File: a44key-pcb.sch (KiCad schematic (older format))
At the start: 61 parts, among them J1 AudioJack3, SW1 SW_Push, U1 ATmega32U4-AU, Y1 16MHz

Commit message: Added raisers for the thumbs
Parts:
- added J2, J3: Conn_01x04_Female, Connector_PinHeader_2.54mm:PinHeader_1x04_P2.54mm_Vertical, symbol Connector:Conn_01x04_Female
- J1: symbol SJ-43514:SJ-43514 -> a44key-pcb-rescue:SJ-43514-SJ-43514
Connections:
- net COL4: now also J2.2 (Pin_2)
- net COL5: now also J2.3 (Pin_3)
- net GND: now also Y1.2, Y1.4; no longer Y1.1, Y1.3
- net at C3.1, U1.16 (XTAL2): now also Y1.3; no longer Y1.2
- net at C2.1, U1.17 (XTAL1): now also Y1.1; no longer Y1.4
- net TH35: now reaches D4.2 (A), MX4.2 (ROW)
- net TH35: now also J3.2 (Pin_2)
- net TH34: now reaches D8.2 (A), MX8.2 (ROW)
- net TH34: now also J3.3 (Pin_3)
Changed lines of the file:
@@
 Wire Wire Line
 	3000 3050 2700 3050
-$Comp
-L Device:Crystal_GND24_Small Y1
-U 1 1 616C3379
-P 2150 2550
-F 0 "Y1" H 2294 2596 50  0000 L CNN
-F 1 "16MHz" H 2294 2505 50  0000 L CNN
-F 2 "Crystal:Crystal_SMD_3225-4Pin_3.2x2.5mm_HandSoldering" H 2150 2550 50  0001 C CNN
-F 3 "~" H 2150 2550 50  0001 C CNN
-	1    2150 2550
-	1    0    0    -1
-$EndComp
 Wire Wire Line
 	3000 2450 2150 2450
@@
 ROW3
 $Comp
-L SJ-43514:SJ-43514 J1
+L a44key-pcb-rescue:SJ-43514-SJ-43514 J1
 U 1 1 6186D5DF
 P 3850 850
@@
 	6450 1200 6750 1200
 $Comp
-L power:+5V #PWR?
+L power:+5V #PWR0115
 U 1 1 617476F1
 P 4500 750
-F 0 "#PWR?" H 4500 600 50  0001 C CNN
+F 0 "#PWR0115" H 4500 600 50  0001 C CNN
 F 1 "+5V" H 4515 923 50  0000 C CNN
 F 2 "" H 4500 750 50  0001 C CNN
@@
 Wire Wire Line
 	4250 750  4500 750
+$Comp
+L Device:Crystal_GND24_Small Y1
+U 1 1 616C3379
+P 2150 2550
+F 0 "Y1" H 2294 2596 50  0000 L CNN
+F 1 "16MHz" H 2294 2505 50  0000 L CNN
+F 2 "Crystal:Crystal_SMD_3225-4Pin_3.2x2.5mm_HandSoldering" H 2150 2550 50  0001 C CNN
+F 3 "~" H 2150 2550 50  0001 C CNN
+	1    2150 2550
+	0    1    1    0
+$EndComp
+$Comp
+L Connector:Conn_01x04_Female J2
+U 1 1 6193A042
+P 6750 5700
+F 0 "J2" H 6642 5275 50  0000 C CNN
+F 1 "Conn_01x04_Female" H 6642 5366 50  0000 C CNN
+F 2 "Connector_PinHeader_2.54mm:PinHeader_1x04_P2.54mm_Vertical" H 6750 5700 50  0001 C CNN
+F 3 "~" H 6750 5700 50  0001 C CNN
+	1    6750 5700
+	1    0    0    1
+$EndComp
+$Comp
+L Connector:Conn_01x04_Female J3
+U 1 1 6193AE0A
+P 8500 5650
+F 0 "J3" H 8528 5626 50  0000 L CNN
+F 1 "Conn_01x04_Female" H 8528 5535 50  0000 L CNN
+F 2 "Connector_PinHeader_2.54mm:PinHeader_1x04_P2.54mm_Vertical" H 8500 5650 50  0001 C CNN
+F 3 "~" H 8500 5650 50  0001 C CNN
+	1    8500 5650
+	1    0    0    -1
+$EndComp
+Text GLabel 6150 5600 0    50   Input ~ 0
+COL5
+Text GLabel 6150 5700 0    50   Input ~ 0
+COL4
+Wire Wire Line
+	6150 5600 6550 5600
+Wire Wire Line
+	6150 5700 6550 5700
+Text GLabel 8000 5650 0    50   Input ~ 0
+TH35
+Text GLabel 8000 5750 0    50   Input ~ 0
+TH34
+Wire Wire Line
+	8000 5650 8300 5650
+Wire Wire Line
+	8000 5750 8300 5750
+Text GLabel 6300 4800 0    50   Input ~ 0
+TH35
+Wire Wire Line
+	6300 4800 6500 4800
+Wire Wire Line
+	6500 4800 6500 4900
+Wire Wire Line
+	6500 4900 6550 4900
+Connection ~ 6550 4900
+Text GLabel 7100 4850 0    50   Input ~ 0
+TH34
+Wire Wire Line
+	7100 4850 7250 4850
+Wire Wire Line
+	7250 4850 7250 4900
+Connection ~ 7250 4900
 $EndSCHEMATC

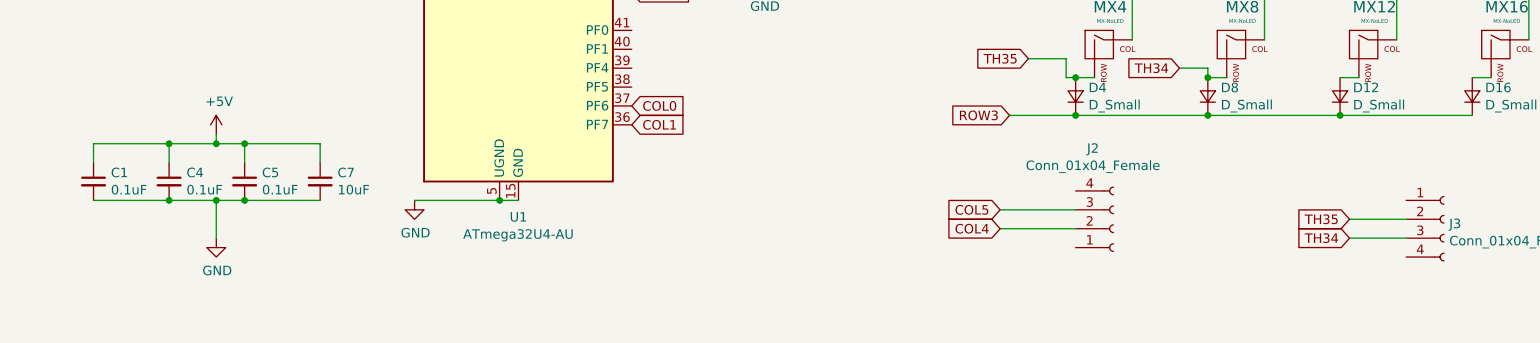
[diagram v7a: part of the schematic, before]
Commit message: Rerouting
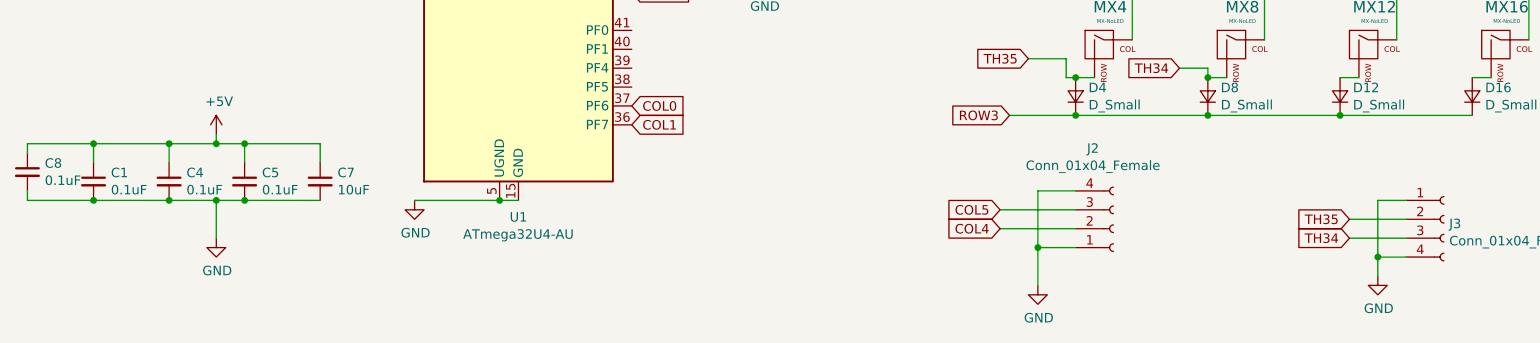
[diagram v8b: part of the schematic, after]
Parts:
- added C8: 0.1uF, Capacitor_SMD:C_0805_2012Metric, symbol Device:C_Small
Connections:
- net +5V: now also C8.1
- net GND: now also J2.1 (Pin_1), J2.4 (Pin_4), J3.1 (Pin_1), J3.4 (Pin_4), C8.2
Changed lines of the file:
@@
 	7250 4850 7250 4900
 Connection ~ 7250 4900
+$Comp
+L Device:C_Small C8
+U 1 1 6197A27B
+P 1000 5400
+F 0 "C8" H 1092 5446 50  0000 L CNN
+F 1 "0.1uF" H 1092 5355 50  0000 L CNN
+F 2 "Capacitor_SMD:C_0805_2012Metric" H 1000 5400 50  0001 C CNN
+F 3 "~" H 1000 5400 50  0001 C CNN
+	1    1000 5400
+	1    0    0    -1
+$EndComp
+Wire Wire Line
+	1350 5550 1000 5550
+Wire Wire Line
+	1000 5550 1000 5500
+Connection ~ 1350 5550
+Wire Wire Line
+	1350 5250 1000 5250
+Wire Wire Line
+	1000 5250 1000 5300
+Connection ~ 1350 5250
+$Comp
+L power:GND #PWR?
+U 1 1 61993731
+P 6350 6000
+F 0 "#PWR?" H 6350 5750 50  0001 C CNN
+F 1 "GND" H 6355 5827 50  0000 C CNN
+F 2 "" H 6350 6000 50  0001 C CNN
+F 3 "" H 6350 6000 50  0001 C CNN
+	1    6350 6000
+	1    0    0    -1
+$EndComp
+$Comp
+L power:GND #PWR?
+U 1 1 61993FD0
+P 8150 5950
+F 0 "#PWR?" H 8150 5700 50  0001 C CNN
+F 1 "GND" H 8155 5777 50  0000 C CNN
+F 2 "" H 8150 5950 50  0001 C CNN
+F 3 "" H 8150 5950 50  0001 C CNN
+	1    8150 5950
+	1    0    0    -1
+$EndComp
+Wire Wire Line
+	8300 5550 8150 5550
+Wire Wire Line
+	8150 5550 8150 5850
+Wire Wire Line
+	8300 5850 8150 5850
+Connection ~ 8150 5850
+Wire Wire Line
+	8150 5850 8150 5950
+Wire Wire Line
+	6550 5500 6350 5500
+Wire Wire Line
+	6350 5500 6350 5800
+Wire Wire Line
+	6550 5800 6350 5800
+Connection ~ 6350 5800
+Wire Wire Line
+	6350 5800 6350 6000
 $EndSCHEMATC
